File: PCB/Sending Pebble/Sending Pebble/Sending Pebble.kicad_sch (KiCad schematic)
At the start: 54 parts, among them J1 USB_C_Receptacle_USB2.0_16P, J2 Conn_01x02_Socket, J3 u.Fl, J4 SMA, J5 Conn_01x03_Socket, Q1 IRLML0030, U1 LoRa-E5, U2 TPS63001, U3 MAX-M10S, U4 BMP390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

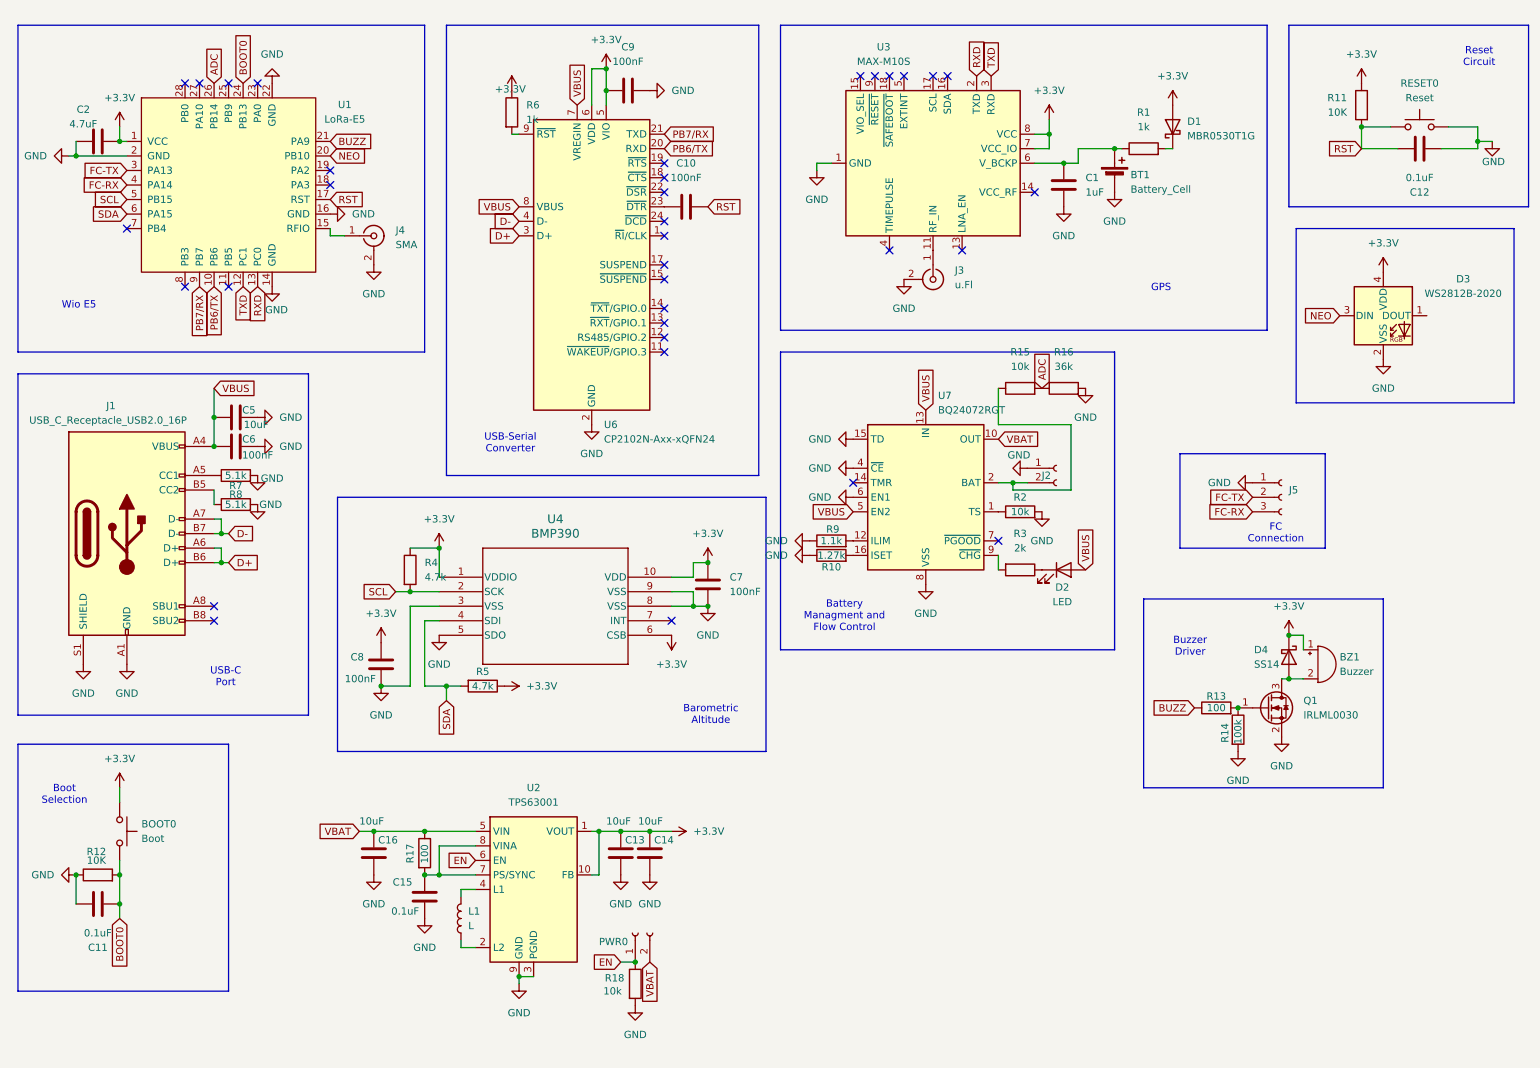
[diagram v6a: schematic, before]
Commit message: More routing, added amplifier connector, fixed coplanar waveguide. Started adding graphics
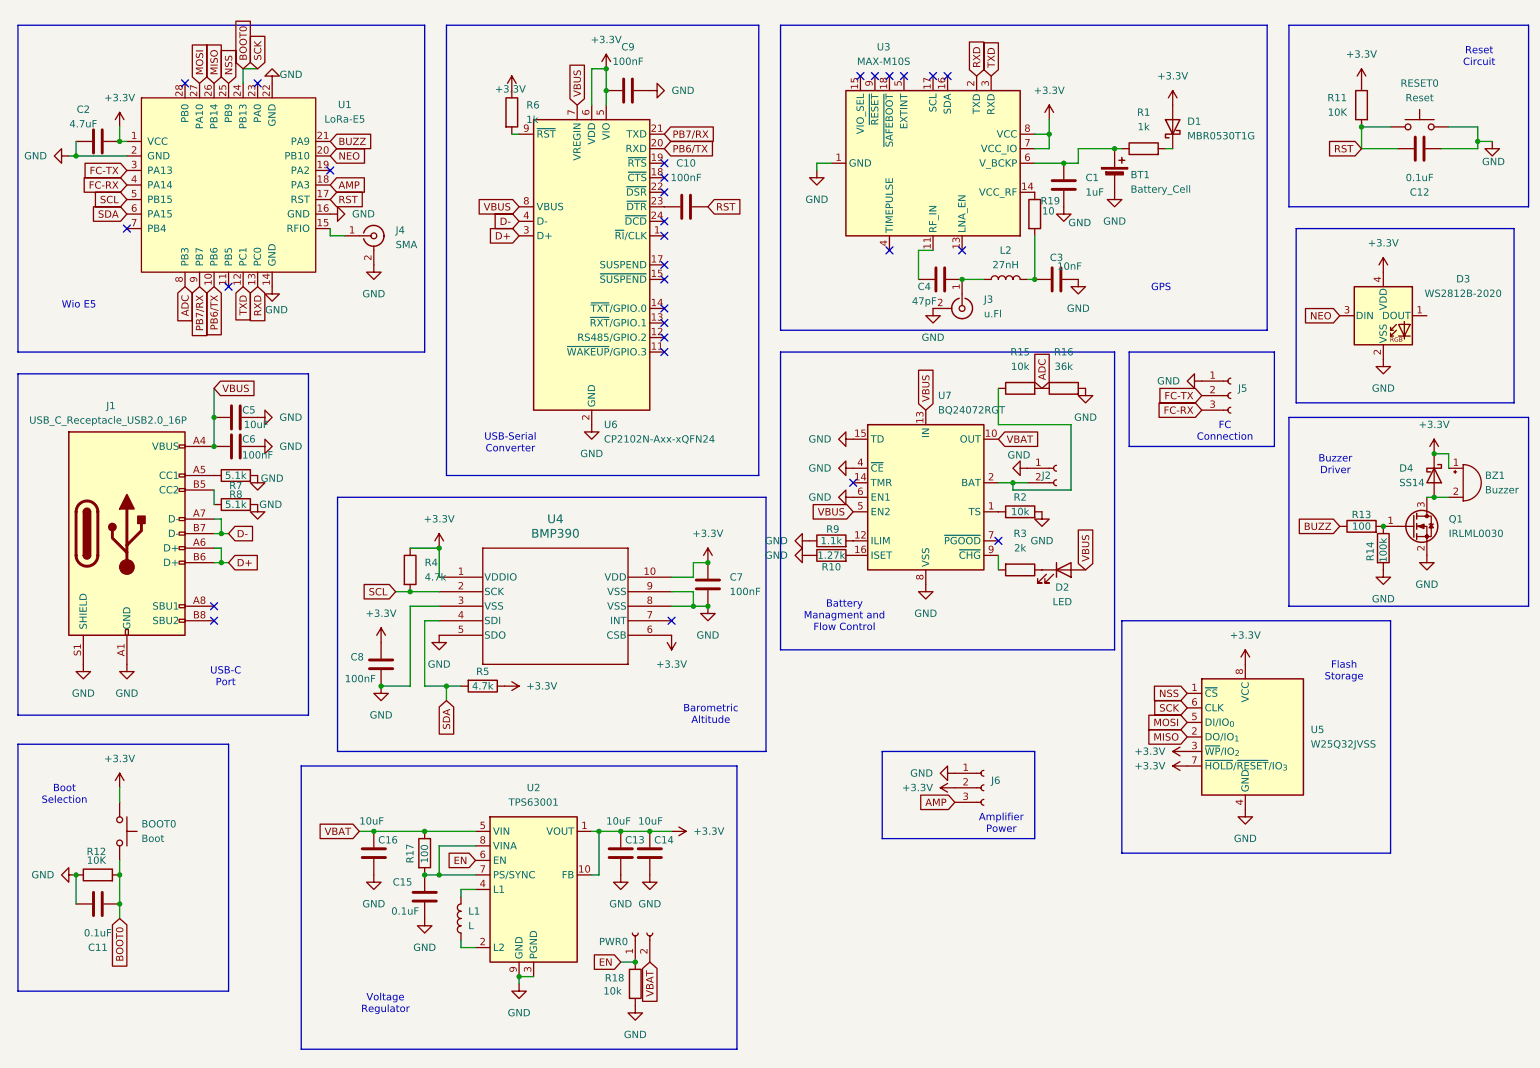
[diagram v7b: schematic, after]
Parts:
- added C3: 10nF, Capacitor_SMD:C_0402_1005Metric, symbol Device:C
- added C4: 47pF, Capacitor_SMD:C_0402_1005Metric, symbol Device:C
- added J6: Conn_01x03_Socket, Connector_PinHeader_2.54mm:PinHeader_1x03_P2.54mm_Vertical, symbol Connector:Conn_01x03_Socket
- added L2: 27nH, Capacitor_SMD:C_0402_1005Metric, symbol Device:L
- added R19: 10, Capacitor_SMD:C_0402_1005Metric, symbol Device:R
- added U5: W25Q32JVSS, Package_SO:SOIC-8_5.3x5.3mm_P1.27mm, symbol Memory_Flash:W25Q32JVSS
- J5: footprint (none) -> Connector_JST:JST_XH_B3B-XH-AM_1x03_P2.50mm_Vertical
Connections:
- net +3.3V: now also J6.2 (Pin_2), U5.3 (~{WP}/IO_{2}), U5.7 (~{HOLD}/~{RESET}/IO_{3}), U5.8 (VCC)
- net ADC: now also U1.8 (PB3); no longer U1.26 (PB14)
- net BOOT0: now also U5.6 (CLK)
- net GND: now also C3.2, J6.1 (Pin_1), U5.4 (GND)
- net AMP: now reaches U1.18 (PA3)
- net AMP: now also J6.3 (Pin_3)
- net NSS: now reaches U1.25 (PB9)
- net NSS: now also U5.1 (~{CS})
- net MOSI: now reaches U1.27 (PA10)
- net MOSI: now also U5.5 (DI/IO_{0})
- net at J3.1 (In): now also C4.2, L2.1; no longer U3.11 (RF_IN)
- net at U3.14 (VCC_RF): now also R19.1
- new net: C3.1, L2.2, R19.2
- new net: C4.1, U3.11 (RF_IN)
- new net MISO: U1.26 (PB14), U5.2 (DO/IO_{1})
- no-connect marks 34 -> 29
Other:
- note added: "Amplifier Power"
- note added: "Flash Storage"
- note added: "Voltage Regulator"
- moved on the sheet: BZ1, D4, J3, J5, Q1, R13, R14
